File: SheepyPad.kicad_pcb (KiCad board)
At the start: 2 copper layers, 127.6 x 99.1 mm, 46 parts, among them SW1 SW_Push, SW2 Rotary_Encoder_Switch, U1 Sparkfun_Pro_Micro

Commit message: Various Updates
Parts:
- added D22: WS2812B, LED_SMD:LED_WS2812B_PLCC4_5.0x5.0mm_P3.2mm, B.Cu at (69.8, 56.5)
- added D23: WS2812B, LED_SMD:LED_WS2812B_PLCC4_5.0x5.0mm_P3.2mm, B.Cu at (177.2, 121.3)
- added D24: WS2812B, LED_SMD:LED_WS2812B_PLCC4_5.0x5.0mm_P3.2mm, B.Cu at (80.6, 93.3)
- added D25: WS2812B, LED_SMD:LED_WS2812B_PLCC4_5.0x5.0mm_P3.2mm, B.Cu at (177.2, 64.8)
- added D26: WS2812B, LED_SMD:LED_WS2812B_PLCC4_5.0x5.0mm_P3.2mm, B.Cu at (112.4, 121.3)
- added D27: WS2812B, LED_SMD:LED_WS2812B_PLCC4_5.0x5.0mm_P3.2mm, B.Cu at (112.4, 65.4)
- added G***: LOGO, Logos:IronMan, F.Cu at (80.0, 90.8)
- added G***: LOGO, Logos:Sheepy, F.Cu at (96.5, 74.3)
- moved R1 8.98 mm to (76.8, 58.4)
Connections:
- U1 pad 13: /ROW_1 -> /COL_4
- U1 pad 14: Net-(U1-Pad14) -> /COL_3
- U1 pad 15: Net-(U1-Pad15) -> /COL_2
- U1 pad 16: Net-(U1-Pad16) -> /COL_1
- U1 pad 17: Net-(U1-Pad17) -> /ROW_1
- U1 pad 18: Net-(U1-Pad18) -> /GLOW_LED
- U1 pad 19: /SCL -> /SDA
- U1 pad 20: /SDA -> /SCL
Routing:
- net /COL_4: track 89.5 -> 166.9 mm, vias 0 -> 1
- net /COL_3: track 89.5 -> 151.5 mm, vias 0 -> 1
- net Net-(D25-Pad2): track 0.00 -> 61.5 mm, vias 0 -> 2
- net Net-(D23-Pad4): track 0.00 -> 61.2 mm
- net Net-(D23-Pad2): track 0.00 -> 60.7 mm
- net Net-(D22-Pad2): track 0.00 -> 50.8 mm
- net Net-(D24-Pad2): track 0.00 -> 50.1 mm, vias 0 -> 2
- net /COL_2: track 89.5 -> 137.8 mm, vias 0 -> 2
- net /COL_1: track 89.5 -> 120.5 mm, vias 0 -> 1
- net +5V: track 0.00 -> 17.6 mm, vias 0 -> 6
- net /GLOW_LED: track 0.00 -> 16.1 mm
- net /ROW_1: track 79.2 -> 92.0 mm
- net GND: track 0.00 -> 11.2 mm, vias 0 -> 2
- net /RESET: track 29.8 -> 33.3 mm
- net /SDA: track 53.6 -> 56.4 mm
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
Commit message: Update
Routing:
- net /ROW_2: track 102.1 -> 84.1 mm
- net /ROW_3: track 121.5 -> 104.2 mm
- net GND: track 11.2 -> 0.00 mm, vias 2 -> 0
- net Net-(D25-Pad2): vias 2 -> 0

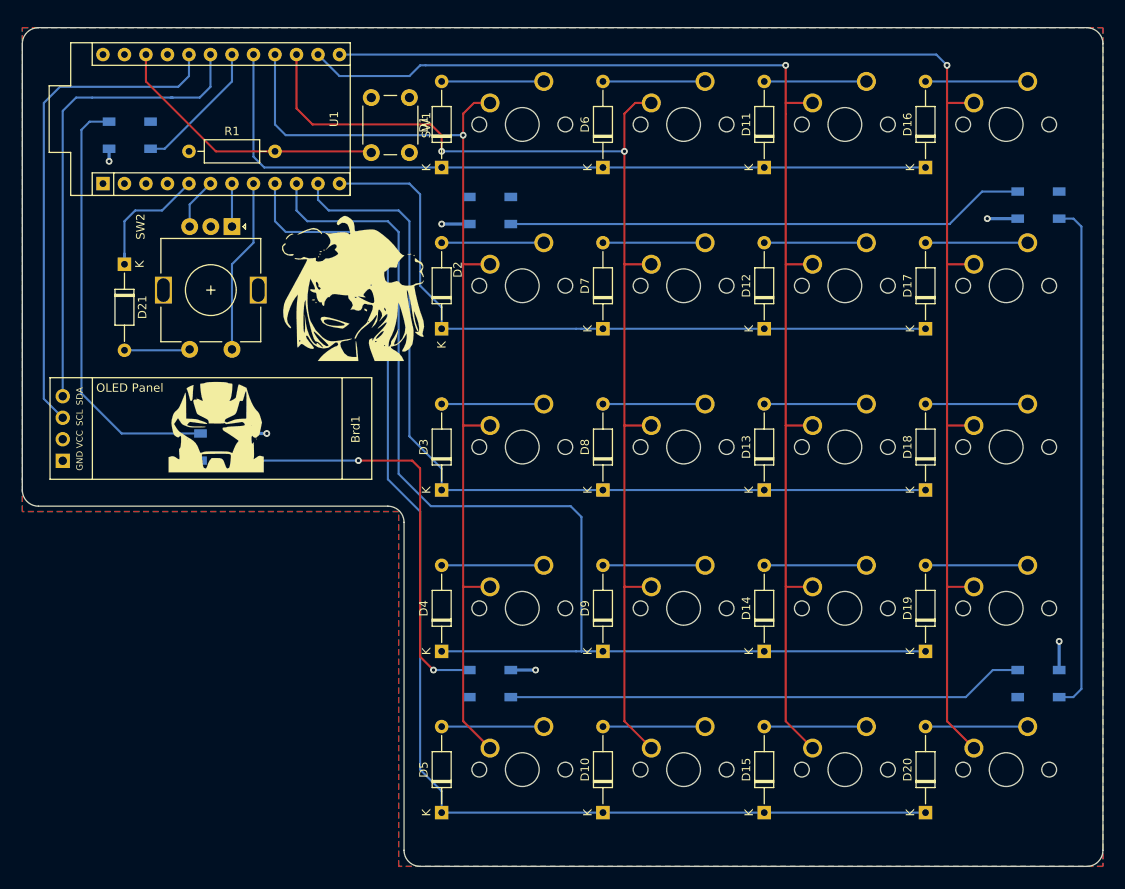
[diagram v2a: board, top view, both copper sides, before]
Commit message: Changes
- Updated silkscreen logos
- Updated tracks
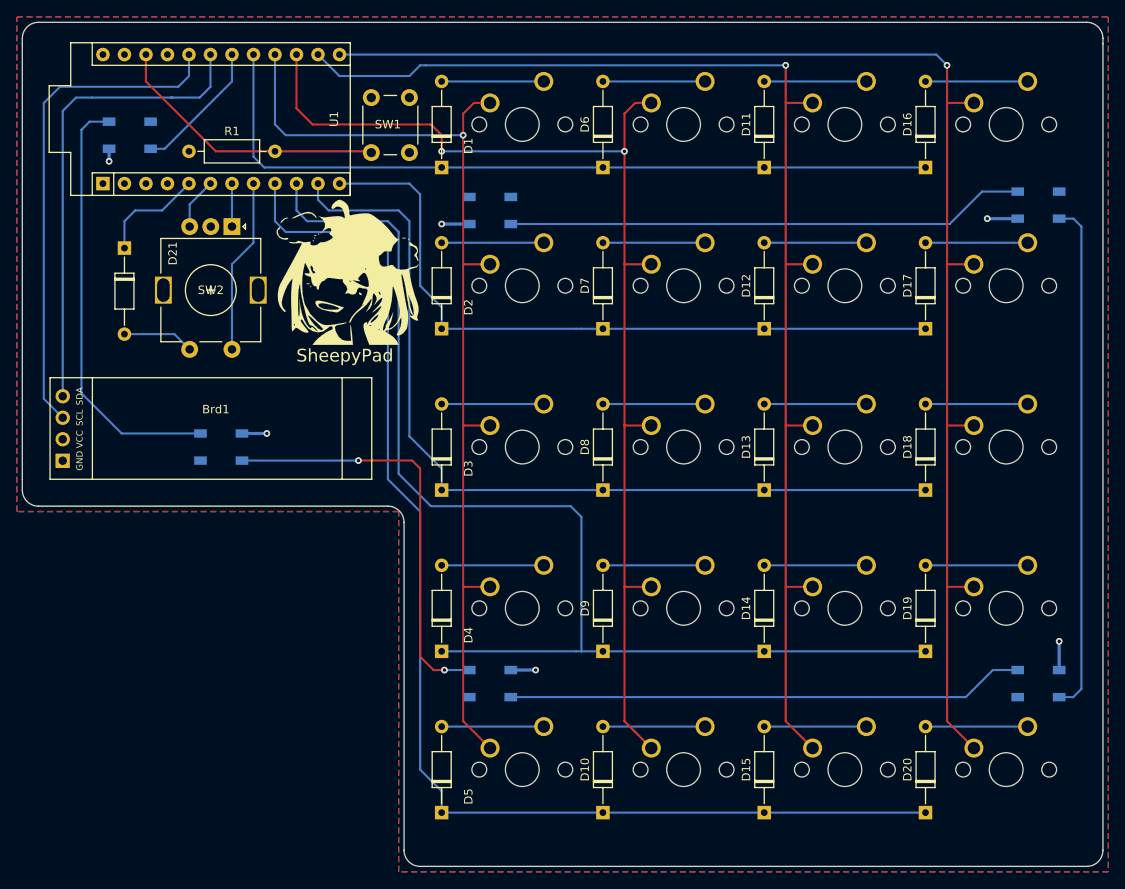
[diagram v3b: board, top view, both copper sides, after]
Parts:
- G***: moved to B.Cu
- moved G*** 19.3 mm to (93.3, 76.8), turned to 180 degrees
- moved G*** 2.01 mm to (95.9, 72.4)
- moved D21 1.91 mm to (69.2, 69.8)
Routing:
- net /COL_ENC_1: track 15.8 -> 12.6 mm
- net Net-(D21-Pad2): track 7.89 -> 8.74 mm
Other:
- board size 127.6 x 99.1 mm -> 127.6 x 99.7 mm
- board text added: "Designed by Cipulot"
- board text added: "SheepyPad"

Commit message: Updates
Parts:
- moved D22 3.70 mm to (66.7, 54.6)
- moved D23 0.64 mm to (177.2, 121.9)
- moved D26 0.64 mm to (112.4, 121.9)
- moved D27 0.64 mm to (112.4, 64.8)
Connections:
- U1 pad 1: Net-(U1-Pad1) -> /ENC_B
- U1 pad 19: /SDA -> Net-(U1-Pad19)
- U1 pad 2: Net-(U1-Pad2) -> /ENC_A
- U1 pad 20: /SCL -> Net-(U1-Pad20)
- U1 pad 5: /COL_ENC_1 -> /SDA
- U1 pad 6: /ENC_B -> /SCL
- U1 pad 7: /ENC_A -> /COL_ENC_1
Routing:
- net /SDA: track 56.4 -> 37.6 mm
- net /SCL: track 59.1 -> 40.8 mm
- net Net-(D22-Pad2): track 50.8 -> 69.0 mm
- net /ENC_A: track 5.08 -> 16.6 mm
- net /COL_ENC_1: track 12.6 -> 22.6 mm
- net /ENC_B: track 6.10 -> 14.2 mm
- net /ROW_ENC_1: track 20.0 -> 25.0 mm
- net /GLOW_LED: track 16.1 -> 21.1 mm
- net Net-(D24-Pad2): track 50.1 -> 51.1 mm
- net Net-(D23-Pad2): track 60.7 -> 61.3 mm
- net +5V: track 17.6 -> 18.2 mm

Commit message: Update
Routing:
- net /COL_3: track 151.5 -> 160.5 mm, vias 1 -> 0
- net /COL_2: track 137.8 -> 144.0 mm, vias 2 -> 0
- net /COL_4: track 166.9 -> 169.3 mm, vias 1 -> 0
- net /COL_1: track 120.5 -> 120.1 mm, vias 1 -> 0

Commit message: Updates
- Updates nets (again)
- Updated gerber files for production
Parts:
- added C1: 100n, Capacitor_THT:C_Disc_D6.0mm_W2.5mm_P5.00mm, F.Cu at (83.2, 88.3)
- added C2: 100n, Capacitor_THT:C_Disc_D6.0mm_W2.5mm_P5.00mm, F.Cu at (120.7, 121.9)
- added C3: 100n, Capacitor_THT:C_Disc_D6.0mm_W2.5mm_P5.00mm, F.Cu at (163.8, 121.9)
- added C4: 100n, Capacitor_THT:C_Disc_D6.0mm_W2.5mm_P5.00mm, F.Cu at (163.8, 64.8)
- added C5: 100n, Capacitor_THT:C_Disc_D6.0mm_W2.5mm_P5.00mm, F.Cu at (125.7, 64.1)
- added C6: 100n, Capacitor_THT:C_Disc_D5.0mm_W2.5mm_P5.00mm, F.Cu at (64.1, 58.4)
- moved D22 1.27 mm to (66.7, 53.3)
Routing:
- net Net-(D22-Pad2): track 69.0 -> 70.3 mm
- net /GLOW_LED: track 21.1 -> 19.8 mm
